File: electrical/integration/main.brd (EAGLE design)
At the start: 168 x 104 mm, 115 parts

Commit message: increment
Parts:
- renumbered JETSON1:X1 to X101, SENSOR_TOP1:U1 to U301

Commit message: clear drc
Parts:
- removed JETSON1:JETSON_J17_UART1:JP2: (no value), pinhead:1X06
- moved MICROCONTROLLER1:R10 4.00 mm to (56.0, -57.7)
- moved MICROCONTROLLER1:R9 4.00 mm to (55.9, -59.4)
- moved MICROCONTROLLER1:U1 4.00 mm to (56.0, -51.1)
- moved MICROCONTROLLER1:LED1 2.00 mm to (40.1, -60.1)
- moved MICROCONTROLLER1:LED2 2.00 mm to (40.1, -56.1)
- moved MICROCONTROLLER1:LED3 2.00 mm to (40.1, -52.0)
- moved MICROCONTROLLER1:LED4 2.00 mm to (40.1, -48.0)
- moved MICROCONTROLLER1:LED5 2.00 mm to (40.1, -46.0)
- moved MICROCONTROLLER1:LED6 2.00 mm to (40.1, -50.0)
- moved MICROCONTROLLER1:LED7 2.00 mm to (40.1, -54.1)
- moved MICROCONTROLLER1:LED8 2.00 mm to (40.1, -58.1)
- moved MICROCONTROLLER1:R1 2.00 mm to (45.5, -60.1)
- moved MICROCONTROLLER1:R2 2.00 mm to (45.5, -56.1)
- moved MICROCONTROLLER1:R3 2.00 mm to (45.5, -52.0)
- moved MICROCONTROLLER1:R4 2.00 mm to (45.5, -48.0)
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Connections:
- net GND: no longer JETSON1:JETSON_J17_UART1:JP2.1
- net N$28: no longer JETSON1:JETSON_J17_UART1:JP2.5
- net N$29: no longer JETSON1:JETSON_J17_UART1:JP2.4
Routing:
- net 3V3: track 159.6 -> 165.4 mm, vias 7 -> 8
- net GND_ISO: track 34.3 -> 29.6 mm, vias 6 -> 7
- net N$28: track 120.6 -> 117.0 mm
- net N$29: track 120.0 -> 116.3 mm
- net MICROCONTROLLER1:N$19: track 6.13 -> 8.47 mm
- net RELAY_CONTROL_TOP1:36V_RAW: track 138.0 -> 136.1 mm
- net RELAY_CONTROL_TOP1:RELAY_CONTROL1:UVLO1:N$4: track 6.69 -> 8.56 mm
- net MICROCONTROLLER1:N$18: track 8.84 -> 10.6 mm
- net MICROCONTROLLER1:N$2: track 20.0 -> 21.8 mm
- net MICROCONTROLLER1:N$24: track 17.4 -> 19.1 mm
- net MICROCONTROLLER1:LED_SCL: track 72.3 -> 70.7 mm
- net RELAY_CONTROL_TOP1:RELAY_CONTROL1:UVLO1:N$2: track 17.8 -> 18.9 mm
- net MICROCONTROLLER1:N$23: track 15.4 -> 16.5 mm
- net RELAY_CONTROL_TOP1:RELAY_CONTROL1:UVLO1:N$3: track 11.3 -> 12.3 mm
- net 5V_ISO: track 96.0 -> 97.0 mm
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- added copper zone on layer 1, net GND_ISO

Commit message: clean routing
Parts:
- moved RELAY_CONTROL_TOP1:R1 1.70 mm to (38.8, -13.8)
- moved RELAY_CONTROL_TOP1:REGULATOR1:U1 1.30 mm to (47.9, -14.1)
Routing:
- net JETSON1:JETSON_TX2_J21_EXPANSION1:VDD_3V3_SYS: track 50.9 -> 57.2 mm
- net RELAY_CONTROL_TOP1:N$6: track 29.7 -> 24.4 mm
- net N$9: track 102.4 -> 98.8 mm, vias 7 -> 6
- net RELAY_CONTROL_TOP1:RELAY_CONTROL1:!UVLO!: track 84.7 -> 83.4 mm
- net N$18: track 88.8 -> 89.8 mm, vias 5 -> 4
- net RELAY_CONTROL_TOP1:N$3: track 37.7 -> 38.7 mm
- net GND_ISO: track 29.6 -> 30.3 mm
- net N$32: track 20.3 -> 21.0 mm
- net N$17: track 95.1 -> 94.4 mm
- net RELAY_CONTROL_TOP1:36V_RAW: track 136.1 -> 135.4 mm
- net N$8: track 150.3 -> 149.7 mm
- net JETSON1:JETSON_TX2_J21_EXPANSION1:N$5: track 3.94 -> 3.39 mm
- net RELAY_CONTROL_TOP1:N$5: track 67.8 -> 68.3 mm
- net N$25: track 71.6 -> 71.7 mm, vias 3 -> 2

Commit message: add silk for connectors and leds
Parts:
- moved POWER_TOP1:R4 14.2 mm to (-31.1, 1.46), turned to 180 degrees
- moved POWER_TOP1:LED1 6.76 mm to (-25.7, 1.40), turned to 0 degrees
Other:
- board text added: "BAT"
- board text added: "BAT IN"
- board text added: "DECK 1"
- board text added: "DECK 2"
- board text added: "DECK 3"
- board text added: "DRV REL"
- board text added: "ENC LFT"
- board text added: "ENC RT"
- board text added: "ESTOP"
- board text added: "GPS UART"
- board text added: "ISO"
- board text added: "LED_12V"
- board text added: "LED_36V"
- board text added: "LED_5V"
- board text added: "MOW EN"
- board text added: "MOW REL"
- board text added: "MRT LFT"
- board text added: "MTR RT"
- board text added: "RCRX"
- board text added: "TETHER"
- board text added: "TX2_12V"
- board text added: "tx2LED1 tx2LED2 tx2LED3 tx2LED4 tx2LED5 tx2LED6 tx2LED7 tx2LED8"
- board text added: "ucLED1 ucLED2 ucLED3 ucLED4 ucLED5 ucLED6 ucLED7 ucLED8"

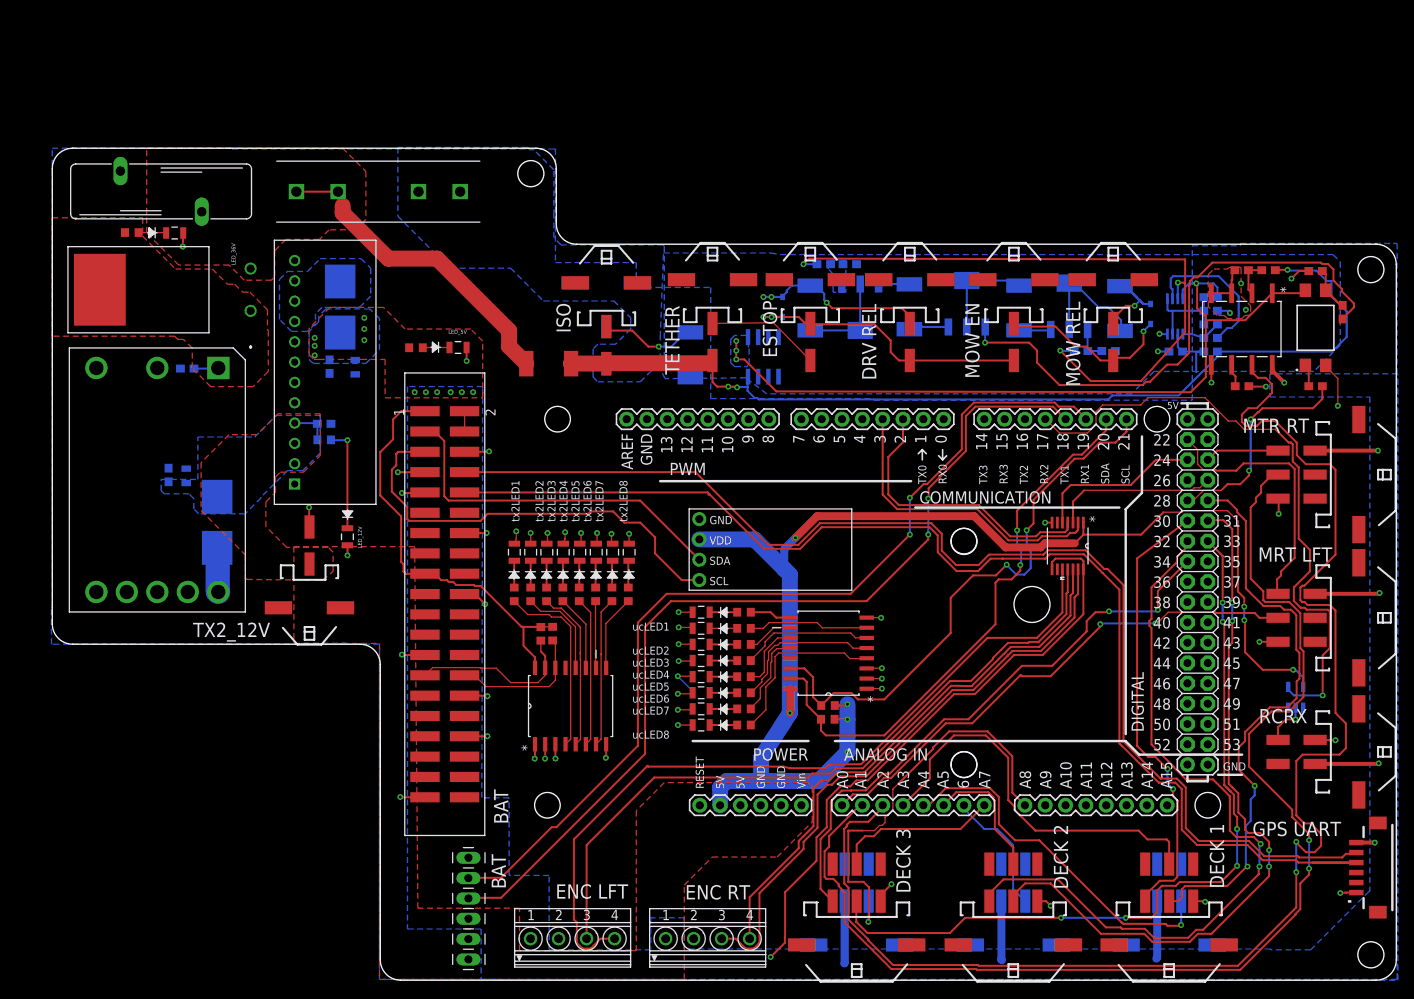
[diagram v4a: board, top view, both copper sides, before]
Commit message: fix broken motor schematic links, ipso facto added to PCB
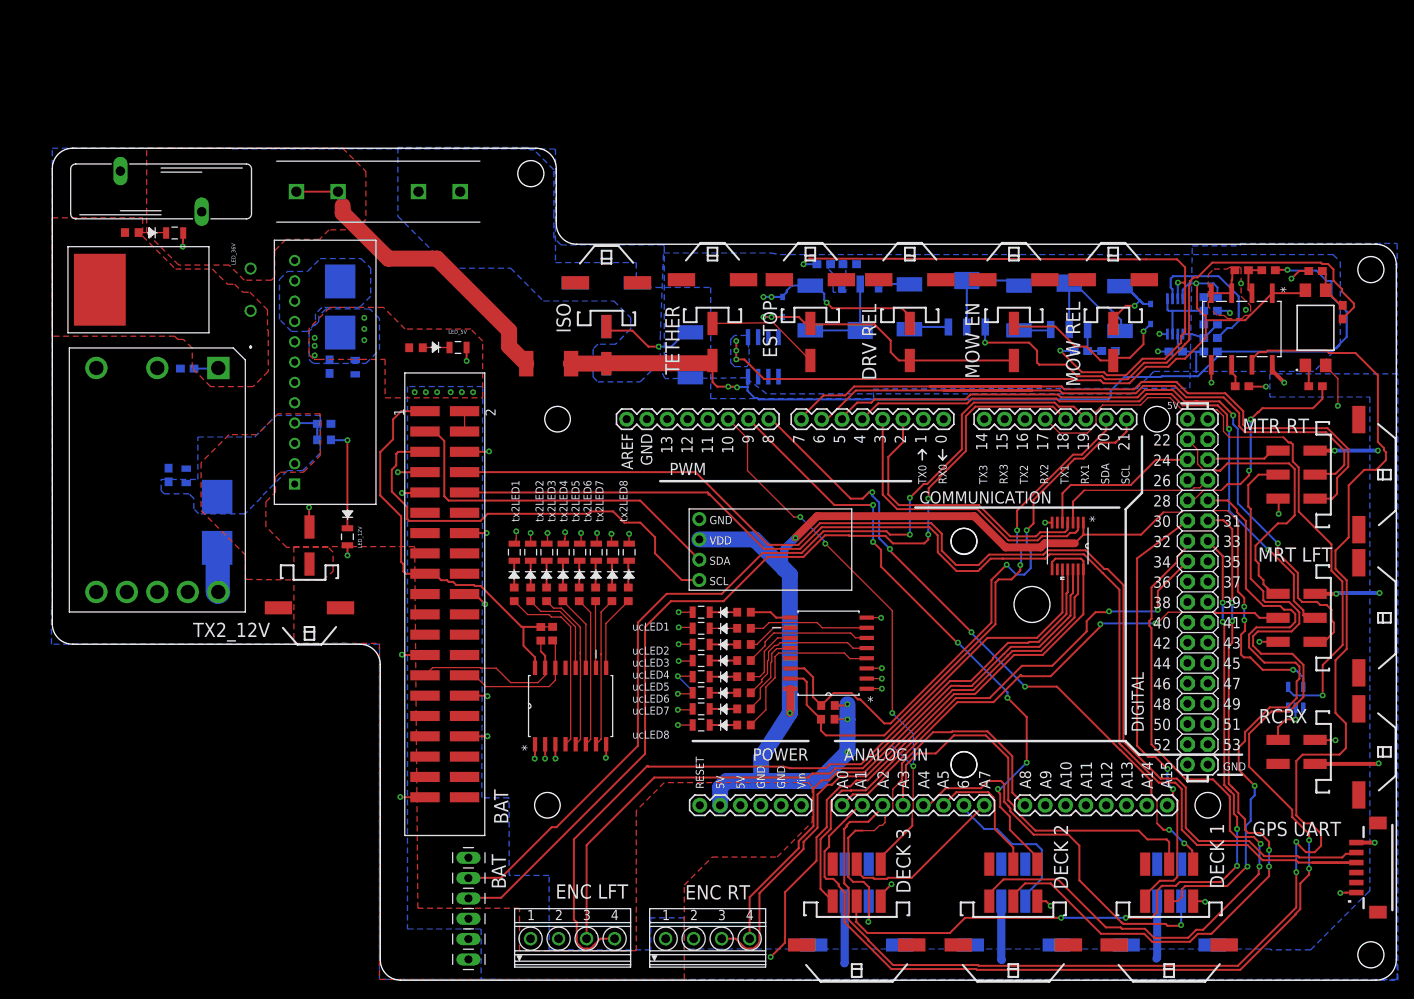
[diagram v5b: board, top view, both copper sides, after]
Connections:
- net MICROCONTROLLER1:N$4 renamed MICROCONTROLLER1:RX0
- removed net MICROCONTROLLER1:N$10: MICROCONTROLLER1:U$1.9
- removed net MICROCONTROLLER1:N$11: MICROCONTROLLER1:U$1.10
- removed net MICROCONTROLLER1:N$5: MICROCONTROLLER1:U$1.4
- removed net MICROCONTROLLER1:N$6: MICROCONTROLLER1:U$1.5
- removed net MICROCONTROLLER1:N$7: MICROCONTROLLER1:U$1.6
- removed net MICROCONTROLLER1:N$8: MICROCONTROLLER1:U$1.7
- removed net MICROCONTROLLER1:N$9: MICROCONTROLLER1:U$1.8
- net N$1: now also MICROCONTROLLER1:U$1.7
- net N$11: now also MICROCONTROLLER1:U$1.10
- net N$16: now also MICROCONTROLLER1:U$1.9
- net N$23: now also MICROCONTROLLER1:U$1.8
- net N$26: now also MICROCONTROLLER1:U$1.5
- net N$27: now also MICROCONTROLLER1:U$1.4
- net N$5: now also MICROCONTROLLER1:U$1.6
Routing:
- net N$1: track 0.00 -> 102.7 mm
- net N$26: track 0.00 -> 89.2 mm, vias 0 -> 2
- net N$5: track 0.00 -> 88.9 mm
- net N$23: track 0.00 -> 83.5 mm, vias 0 -> 6
- net N$27: track 0.00 -> 78.9 mm, vias 0 -> 2
- net N$16: track 0.00 -> 76.7 mm, vias 0 -> 6
- net N$11: track 0.00 -> 71.2 mm, vias 0 -> 4
- net N$8: track 149.7 -> 160.5 mm
- net N$25: track 71.7 -> 81.2 mm
- net N$3: track 33.3 -> 37.8 mm
- net VSENSE: track 178.2 -> 182.1 mm
- net 5V_ISO: track 97.0 -> 93.2 mm
- net N$14: track 16.1 -> 19.6 mm
- net MICROCONTROLLER1:LED_SCL: track 70.7 -> 73.7 mm
- net N$21: track 45.3 -> 48.1 mm
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
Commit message: update libraries for schematic and pcb for synced bom parameters
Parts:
- SENSOR_TOP1:ENCODER1:X1, SENSOR_TOP1:ENCODER2:X1: value 1984989 -> 1751264; device con-phoenix-350:1751264 -> power_connectors:1751264
